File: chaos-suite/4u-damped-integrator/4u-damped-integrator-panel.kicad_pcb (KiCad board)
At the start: 2 copper layers, 50.5 x 175 mm, 1 part

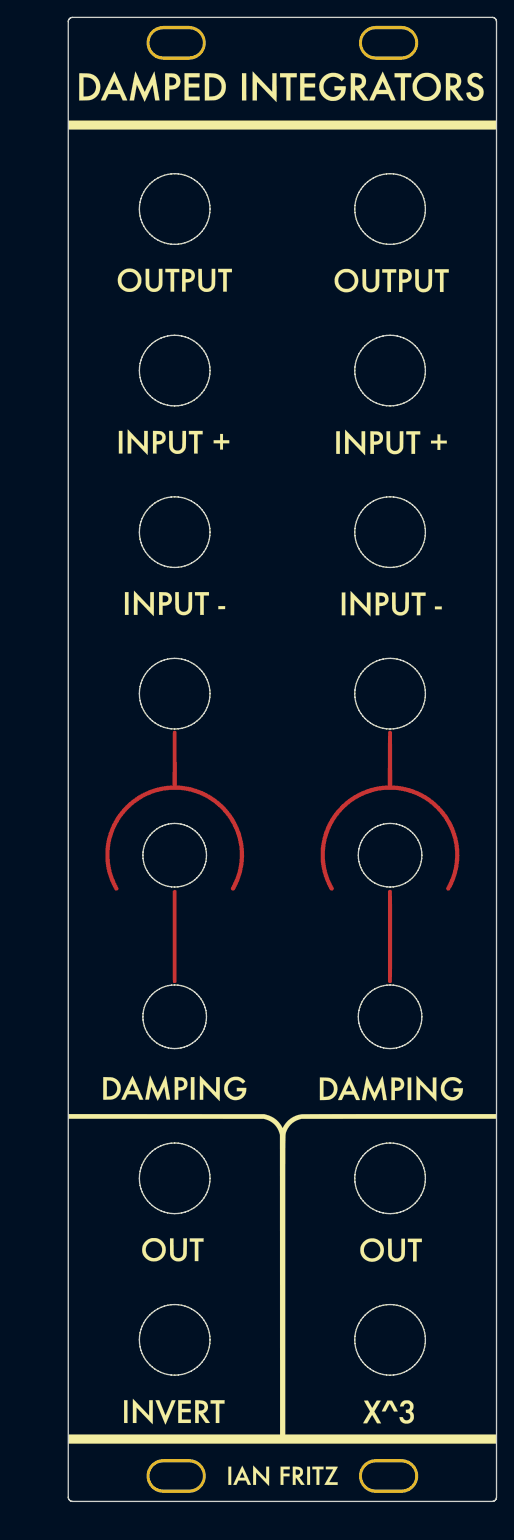
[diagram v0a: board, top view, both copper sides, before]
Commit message: adding more panel stuff for damped integrators
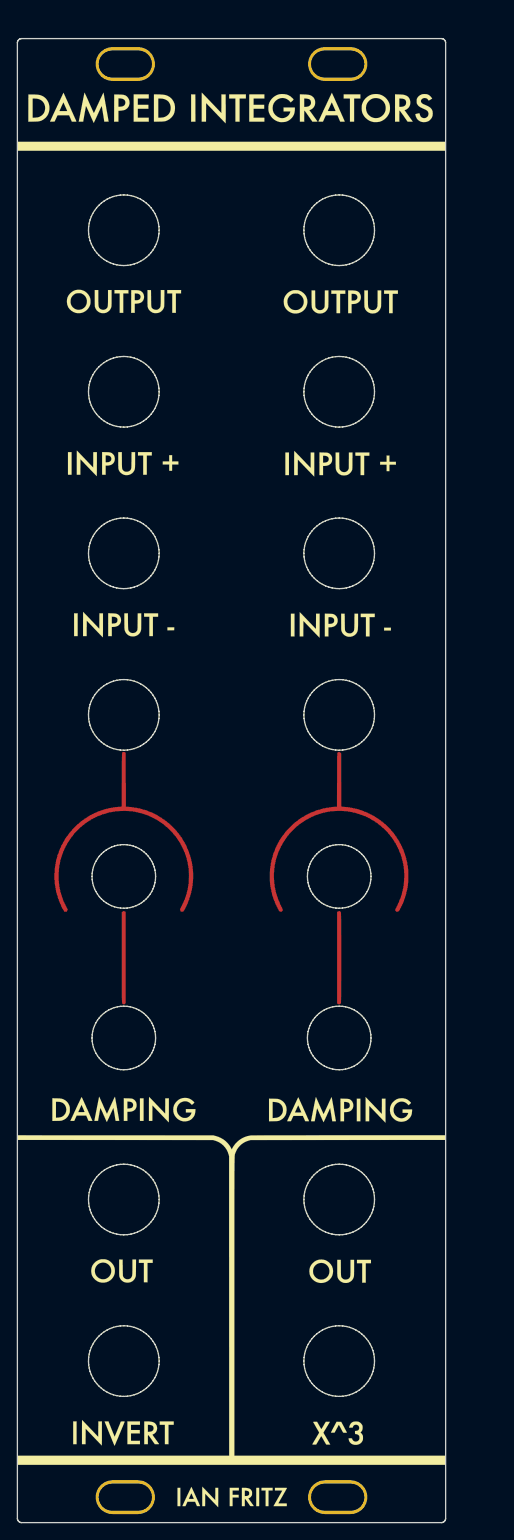
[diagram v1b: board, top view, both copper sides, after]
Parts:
- moved Ref** 6.50 mm to (100.0, 110.0)
